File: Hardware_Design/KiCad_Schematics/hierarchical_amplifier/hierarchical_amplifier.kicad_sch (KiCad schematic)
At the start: 3 parts, among them J1 Screw_Terminal_01x02, J2 Screw_Terminal_01x02, J3 Screw_Terminal_01x02

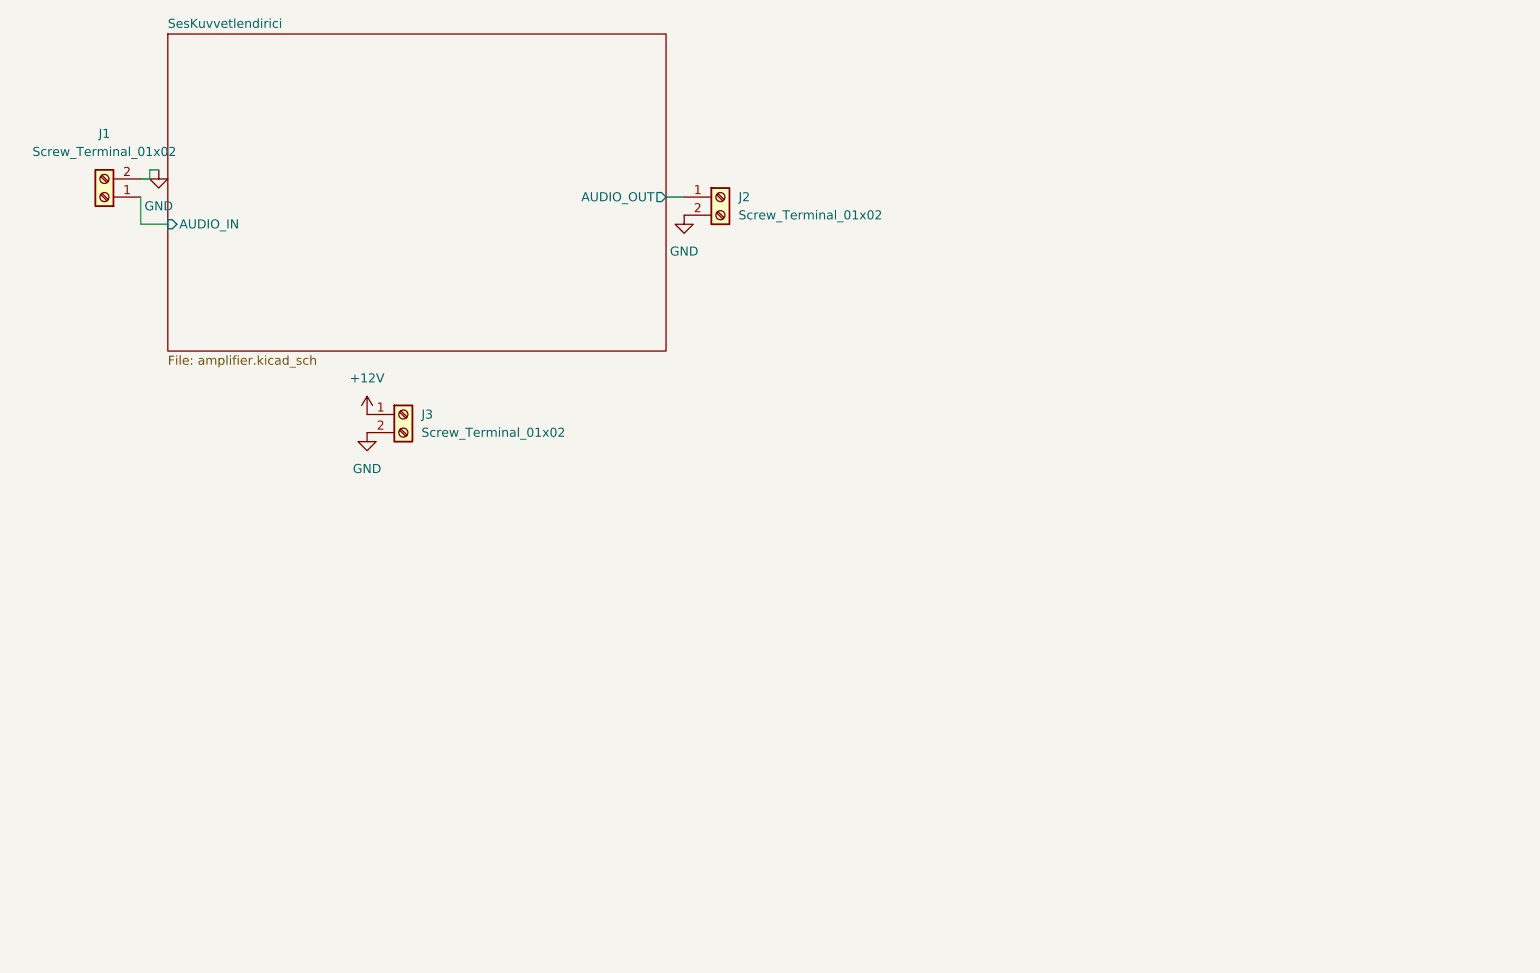
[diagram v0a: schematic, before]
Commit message: Add README for Hierarchical Amplifier circuit
Added the README.md file for the Hierarchical Amplifier project. This file includes the project purpose, component details, functional explanation of the circuit elements (voltage divider, coupling/bypass capacitors), and schematic references to support the hierarchical design documentation.
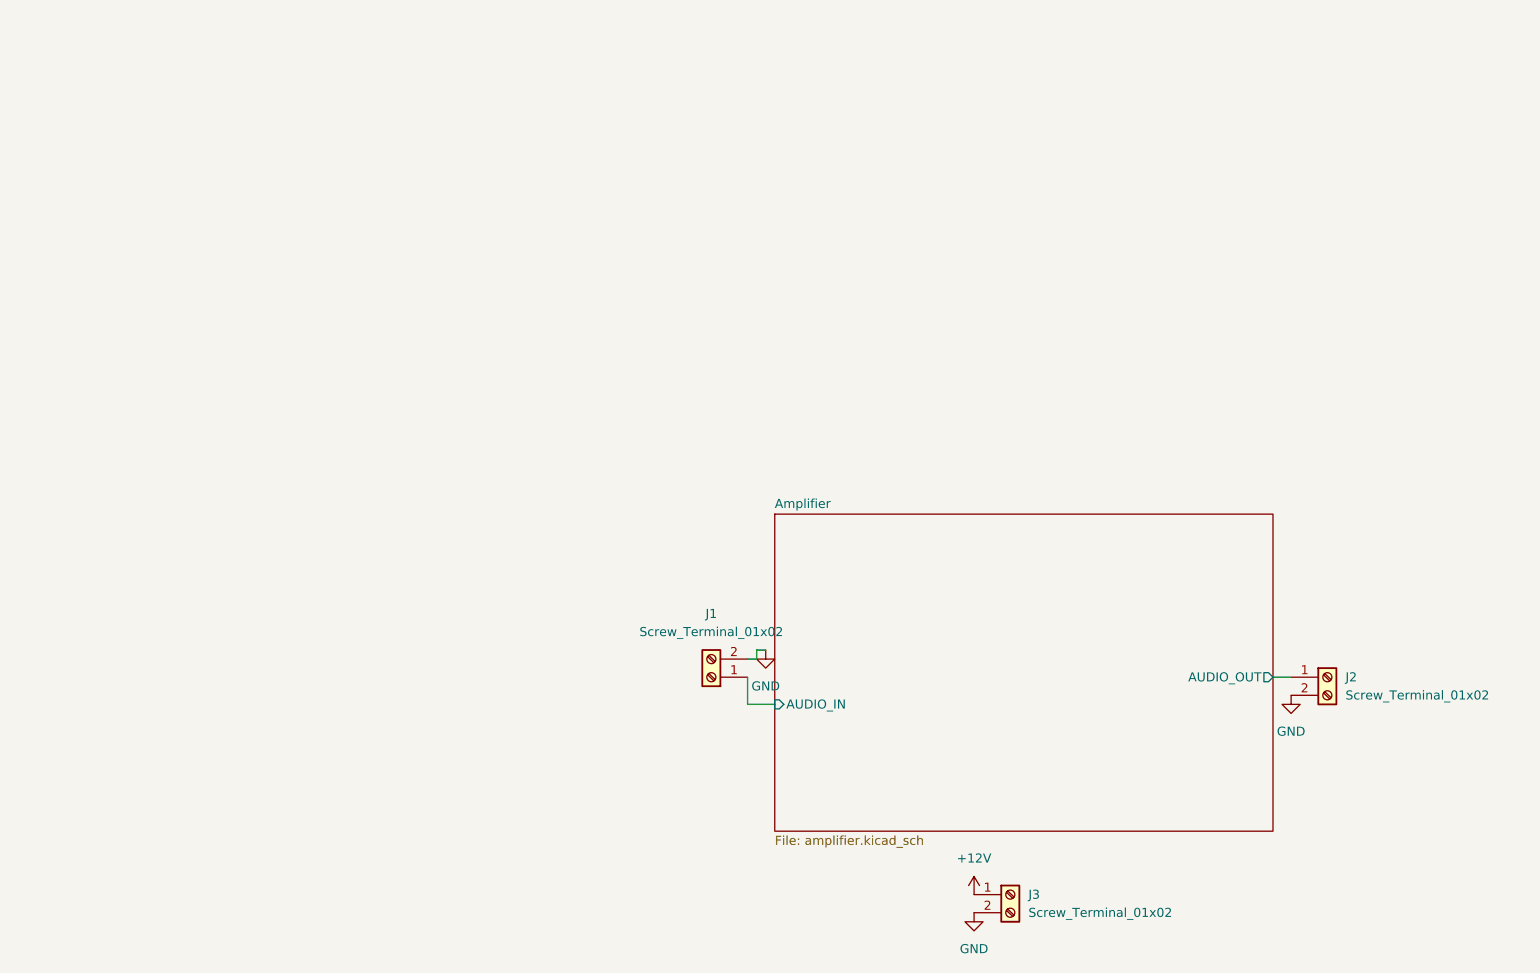
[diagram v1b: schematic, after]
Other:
- sheet SesKuvvetlendirici renamed Amplifier
- moved on the sheet: J1, J2, J3
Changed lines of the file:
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@@
 	(wire
 		(pts
-			(xy 35.56 41.91) (xy 31.75 41.91)
+			(xy 120.65 109.22) (xy 116.84 109.22)
 		)
 		(stroke
@@
 	(wire
 		(pts
-			(xy 31.75 41.91) (xy 31.75 38.1)
+			(xy 116.84 109.22) (xy 116.84 105.41)
 		)
 		(stroke
@@
 	(wire
 		(pts
-			(xy 33.02 34.29) (xy 34.29 34.29)
+			(xy 118.11 101.6) (xy 119.38 101.6)
 		)
 		(stroke
@@
 	(wire
 		(pts
-			(xy 31.75 35.56) (xy 33.02 35.56)
+			(xy 116.84 102.87) (xy 118.11 102.87)
 		)
 		(stroke
@@
 	(wire
 		(pts
-			(xy 105.41 38.1) (xy 107.95 38.1)
+			(xy 190.5 105.41) (xy 193.04 105.41)
 		)
 		(stroke
@@
 	(wire
 		(pts
-			(xy 33.02 35.56) (xy 33.02 34.29)
+			(xy 118.11 102.87) (xy 118.11 101.6)
 		)
 		(stroke
@@
 	(symbol
 		(lib_id "Connector:Screw_Terminal_01x02")
-		(at 113.03 38.1 0)
+		(at 198.12 105.41 0)
 		(unit 1)
 		(body_style 1)
@@
 		(fields_autoplaced yes)
 		(property "Reference" "J2"
-			(at 115.57 38.0999 0)
+			(at 200.66 105.4099 0)
 			(show_name no)
 			(do_not_autoplace no)
@@
 		)
 		(property "Value" "Screw_Terminal_01x02"
-			(at 115.57 40.6399 0)
+			(at 200.66 107.9499 0)
 			(show_name no)
 			(do_not_autoplace no)
@@
 		)
 		(property "Footprint" "TerminalBlock_Phoenix:TerminalBlock_Phoenix_MKDS-1,5-2-5.08_1x02_P5.08mm_Horizontal"
-			(at 113.03 38.1 0)
+			(at 198.12 105.41 0)
 			(hide yes)
 			(show_name no)
@@
 		)
 		(property "Datasheet" ""
-			(at 113.03 38.1 0)
+			(at 198.12 105.41 0)
 			(hide yes)
 			(show_name no)
@@
 		)
 		(property "Description" "Generic screw terminal, single row, 01x02, script generated (kicad-library-utils/schlib/autogen/connector/)"
-			(at 113.03 38.1 0)
+			(at 198.12 105.41 0)
 			(hide yes)
 			(show_name no)
@@
 		)
 		(instances
-			(project "kurs4"
+			(project "hierarchical_amplifier"
 				(path "/1680d475-8d12-44de-9d5b-0889d33728e7"
 					(reference "J2")
@@
 	(symbol
 		(lib_id "Connector:Screw_Terminal_01x02")
-		(at 68.58 68.58 0)
+		(at 153.67 135.89 0)
 		(unit 1)
 		(body_style 1)
@@
 		(fields_autoplaced yes)
 		(property "Reference" "J3"
-			(at 71.12 68.5799 0)
+			(at 156.21 135.8899 0)
 			(show_name no)
 			(do_not_autoplace no)
@@
 		)
 		(property "Value" "Screw_Terminal_01x02"
-			(at 71.12 71.1199 0)
+			(at 156.21 138.4299 0)
 			(show_name no)
 			(do_not_autoplace no)
@@
 		)
 		(property "Footprint" "TerminalBlock_Phoenix:TerminalBlock_Phoenix_MKDS-1,5-2-5.08_1x02_P5.08mm_Horizontal"
-			(at 68.58 68.58 0)
+			(at 153.67 135.89 0)
 			(hide yes)
 			(show_name no)
@@
 		)
 		(property "Datasheet" ""
-			(at 68.58 68.58 0)
+			(at 153.67 135.89 0)
 			(hide yes)
 			(show_name no)
@@
 		)
 		(property "Description" "Generic screw terminal, single row, 01x02, script generated (kicad-library-utils/schlib/autogen/connector/)"
-			(at 68.58 68.58 0)
+			(at 153.67 135.89 0)
 			(hide yes)
 			(show_name no)
@@
 		)
 		(instances
-			(project "kurs4"
+			(project "hierarchical_amplifier"
 				(path "/1680d475-8d12-44de-9d5b-0889d33728e7"
 					(reference "J3")
@@
 	(symbol
 		(lib_id "power:GND")
-		(at 63.5 71.12 0)
+		(at 148.59 138.43 0)
 		(unit 1)
 		(body_style 1)
@@
 		(fields_autoplaced yes)
 		(property "Reference" "#PWR06"
-			(at 63.5 77.47 0)
+			(at 148.59 144.78 0)
 			(hide yes)
 			(show_name no)
@@
 		)
 		(property "Value" "GND"
-			(at 63.5 76.2 0)
+			(at 148.59 143.51 0)
 			(show_name no)
 			(do_not_autoplace no)
@@
 		)
 		(property "Footprint" ""
-			(at 63.5 71.12 0)
+			(at 148.59 138.43 0)
 			(hide yes)
 			(show_name no)
@@
 		)
 		(property "Datasheet" ""
-			(at 63.5 71.12 0)
+			(at 148.59 138.43 0)
 			(hide yes)
 			(show_name no)
@@
 		)
 		(property "Description" "Power symbol creates a global label with name \"GND\" , ground"
-			(at 63.5 71.12 0)
+			(at 148.59 138.43 0)
 			(hide yes)
 			(show_name no)
@@
 		)
 		(instances
-			(project "kurs4"
+			(project "hierarchical_amplifier"
 				(path "/1680d475-8d12-44de-9d5b-0889d33728e7"
 					(reference "#PWR06")
@@
 	(symbol
 		(lib_id "power:+12V")
-		(at 63.5 68.58 0)
+		(at 148.59 135.89 0)
 		(unit 1)
 		(body_style 1)
@@
 		(fields_autoplaced yes)
 		(property "Reference" "#PWR05"
-			(at 63.5 72.39 0)
+			(at 148.59 139.7 0)
 			(hide yes)
 			(show_name no)
@@
 		)
 		(property "Value" "+12V"
-			(at 63.5 63.5 0)
+			(at 148.59 130.81 0)
 			(show_name no)
 			(do_not_autoplace no)
@@
 		)
 		(property "Footprint" ""
-			(at 63.5 68.58 0)
+			(at 148.59 135.89 0)
 			(hide yes)
 			(show_name no)
@@
 		)
 		(property "Datasheet" ""
-			(at 63.5 68.58 0)
+			(at 148.59 135.89 0)
 			(hide yes)
 			(show_name no)
@@
 		)
 		(property "Description" "Power symbol creates a global label with name \"+12V\""
-			(at 63.5 68.58 0)
+			(at 148.59 135.89 0)
 			(hide yes)
 			(show_name no)
@@
 		)
 		(instances
-			(project "kurs4"
+			(project "hierarchical_amplifier"
 				(path "/1680d475-8d12-44de-9d5b-0889d33728e7"
 					(reference "#PWR05")
@@
 	(symbol
 		(lib_id "power:GND")
-		(at 107.95 40.64 0)
+		(at 193.04 107.95 0)
 		(unit 1)
 		(body_style 1)
@@
 		(fields_autoplaced yes)
 		(property "Reference" "#PWR04"
-			(at 107.95 46.99 0)
+			(at 193.04 114.3 0)
 			(hide yes)
 			(show_name no)
@@
 		)
 		(property "Value" "GND"
-			(at 107.95 45.72 0)
+			(at 193.04 113.03 0)
 			(show_name no)
 			(do_not_autoplace no)
@@
 		)
 		(property "Footprint" ""
-			(at 107.95 40.64 0)
+			(at 193.04 107.95 0)
 			(hide yes)
 			(show_name no)
@@
 		)
 		(property "Datasheet" ""
-			(at 107.95 40.64 0)
+			(at 193.04 107.95 0)
 			(hide yes)
 			(show_name no)
@@
 		)
 		(property "Description" "Power symbol creates a global label with name \"GND\" , ground"
-			(at 107.95 40.64 0)
+			(at 193.04 107.95 0)
 			(hide yes)
 			(show_name no)
@@
 		)
 		(instances
-			(project "kurs4"
+			(project "hierarchical_amplifier"
 				(path "/1680d475-8d12-44de-9d5b-0889d33728e7"
 					(reference "#PWR04")
@@
 	(symbol
 		(lib_id "Connector:Screw_Terminal_01x02")
-		(at 26.67 38.1 180)
+		(at 111.76 105.41 180)
 		(unit 1)
 		(body_style 1)
@@
 		(fields_autoplaced yes)
 		(property "Reference" "J1"
-			(at 26.67 29.21 0)
+			(at 111.76 96.52 0)
 			(show_name no)
 			(do_not_autoplace no)
@@
 		)
 		(property "Value" "Screw_Terminal_01x02"
-			(at 26.67 31.75 0)
+			(at 111.76 99.06 0)
 			(show_name no)
 			(do_not_autoplace no)
@@
 		)
 		(property "Footprint" "TerminalBlock_Phoenix:TerminalBlock_Phoenix_MKDS-1,5-2-5.08_1x02_P5.08mm_Horizontal"
-			(at 26.67 38.1 0)
+			(at 111.76 105.41 0)
 			(hide yes)
 			(show_name no)
@@
 		)
 		(property "Datasheet" ""
-			(at 26.67 38.1 0)
+			(at 111.76 105.41 0)
 			(hide yes)
 			(show_name no)
@@
 		)
 		(property "Description" "Generic screw terminal, single row, 01x02, script generated (kicad-library-utils/schlib/autogen/connector/)"
-			(at 26.67 38.1 0)
+			(at 111.76 105.41 0)
 			(hide yes)
 			(show_name no)
@@
 		)
 		(instances
-			(project "kurs4"
+			(project "hierarchical_amplifier"
 				(path "/1680d475-8d12-44de-9d5b-0889d33728e7"
 					(reference "J1")
@@
 	(symbol
 		(lib_id "power:GND")
-		(at 34.29 34.29 0)
+		(at 119.38 101.6 0)
 		(unit 1)
 		(body_style 1)
@@
 		(fields_autoplaced yes)
 		(property "Reference" "#PWR02"
-			(at 34.29 40.64 0)
+			(at 119.38 107.95 0)
 			(hide yes)
 			(show_name no)
@@
 		)
 		(property "Value" "GND"
-			(at 34.29 39.37 0)
+			(at 119.38 106.68 0)
 			(show_name no)
 			(do_not_autoplace no)
@@
 		)
 		(property "Footprint" ""
-			(at 34.29 34.29 0)
+			(at 119.38 101.6 0)
 			(hide yes)
 			(show_name no)
@@
 		)
 		(property "Datasheet" ""
-			(at 34.29 34.29 0)
+			(at 119.38 101.6 0)
 			(hide yes)
 			(show_name no)
@@
 		)
 		(property "Description" "Power symbol creates a global label with name \"GND\" , ground"
-			(at 34.29 34.29 0)
+			(at 119.38 101.6 0)
 			(hide yes)
 			(show_name no)
@@
 		)
 		(instances
-			(project "kurs4"
+			(project "hierarchical_amplifier"
 				(path "/1680d475-8d12-44de-9d5b-0889d33728e7"
 					(reference "#PWR02")
@@
 	)
 	(sheet
-		(at 35.56 15.24)
+		(at 120.65 82.55)
 		(size 69.85 44.45)
 		(exclude_from_sim no)
@@
 			(color 0 0 0 0)
 		)
-		(property "Sheetname" "SesKuvvetlendirici"
-			(at 35.56 14.5284 0)
+		(property "Sheetname" "Amplifier"
+			(at 120.65 81.8384 0)
 			(show_name no)
 			(do_not_autoplace no)
@@
 		)
 		(property "Sheetfile" "amplifier.kicad_sch"
-			(at 35.56 60.2746 0)
+			(at 120.65 127.5846 0)
 			(show_name no)
 			(do_not_autoplace no)
@@
 		)
 		(pin "AUDIO_IN" input
-			(at 35.56 41.91 180)
+			(at 120.65 109.22 180)
 			(effects
 				(font
@@
 		)
 		(pin "AUDIO_OUT" output
-			(at 105.41 38.1 0)
+			(at 190.5 105.41 0)
 			(effects
 				(font
@@
 		)
 		(instances
-			(project "kurs4"
+			(project "hierarchical_amplifier"
 				(path "/1680d475-8d12-44de-9d5b-0889d33728e7"
 					(page "2")

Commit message: feat(hierarchical_amplifier): add info to Symbols Fields Table
Populated MPN, Manufacturer, and LCSC fields in the Symbol Fields Table
to practice using the Bulk Edit Symbol Fields tool in KiCad.
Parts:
- J1, J2, J3: LCSC (none) -> C480516; Manufacturer (none) -> Phoenix Contact; Manufacturer Part Number (none) -> 1715721
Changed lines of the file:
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@@
+			)
+		)
+		(property "LCSC" "C480516"
+			(at 198.12 105.41 0)
+			(hide yes)
+			(show_name no)
+			(do_not_autoplace no)
+			(effects
+				(font
+					(size 1.27 1.27)
+				)
+			)
+		)
+		(property "Manufacturer" "Phoenix Contact"
+			(at 198.12 105.41 0)
+			(hide yes)
+			(show_name no)
+			(do_not_autoplace no)
+			(effects
+				(font
+					(size 1.27 1.27)
+				)
+			)
+		)
+		(property "Manufacturer Part Number" "1715721"
+			(at 198.12 105.41 0)
+			(hide yes)
+			(show_name no)
+			(do_not_autoplace no)
+			(effects
+				(font
+					(size 1.27 1.27)
+				)
 			)
 		)
@@
 			)
 		)
+		(property "LCSC" "C480516"
+			(at 153.67 135.89 0)
+			(hide yes)
+			(show_name no)
+			(do_not_autoplace no)
+			(effects
+				(font
+					(size 1.27 1.27)
+				)
+			)
+		)
+		(property "Manufacturer" "Phoenix Contact"
+			(at 153.67 135.89 0)
+			(hide yes)
+			(show_name no)
+			(do_not_autoplace no)
+			(effects
+				(font
+					(size 1.27 1.27)
+				)
+			)
+		)
+		(property "Manufacturer Part Number" "1715721"
+			(at 153.67 135.89 0)
+			(hide yes)
+			(show_name no)
+			(do_not_autoplace no)
+			(effects
+				(font
+					(size 1.27 1.27)
+				)
+			)
+		)
 		(pin "1"
 		)
@@
 			(at 111.76 105.41 0)
 			(hide yes)
+			(show_name no)
+			(do_not_autoplace no)
+			(effects
+				(font
+					(size 1.27 1.27)
+				)
+			)
+		)
+		(property "LCSC" "C480516"
+			(at 111.76 105.41 0)
+			(hide yes)
+			(show_name no)
+			(do_not_autoplace no)
+			(effects
+				(font
+					(size 1.27 1.27)
+				)
+			)
+		)
+		(property "Manufacturer" "Phoenix Contact"
+			(at 111.76 105.41 0)
+			(hide yes)
+			(show_name no)
+			(do_not_autoplace no)
+			(effects
+				(font
+					(size 1.27 1.27)
+				)
+			)
+		)
+		(property "Manufacturer Part Number" "1715721"
+			(at 111.76 105.41 0)
+			(hide yes)
